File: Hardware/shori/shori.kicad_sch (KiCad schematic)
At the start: 127 parts, among them J1 430450200, J2 SWD_Header, J3 UART_Header, J4 530480310, J5 Conn_01x03, J6 530480210, SW1 SW_SPDT, U1 CS4272, U2 STM32H750VBTx, U3 NE5532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

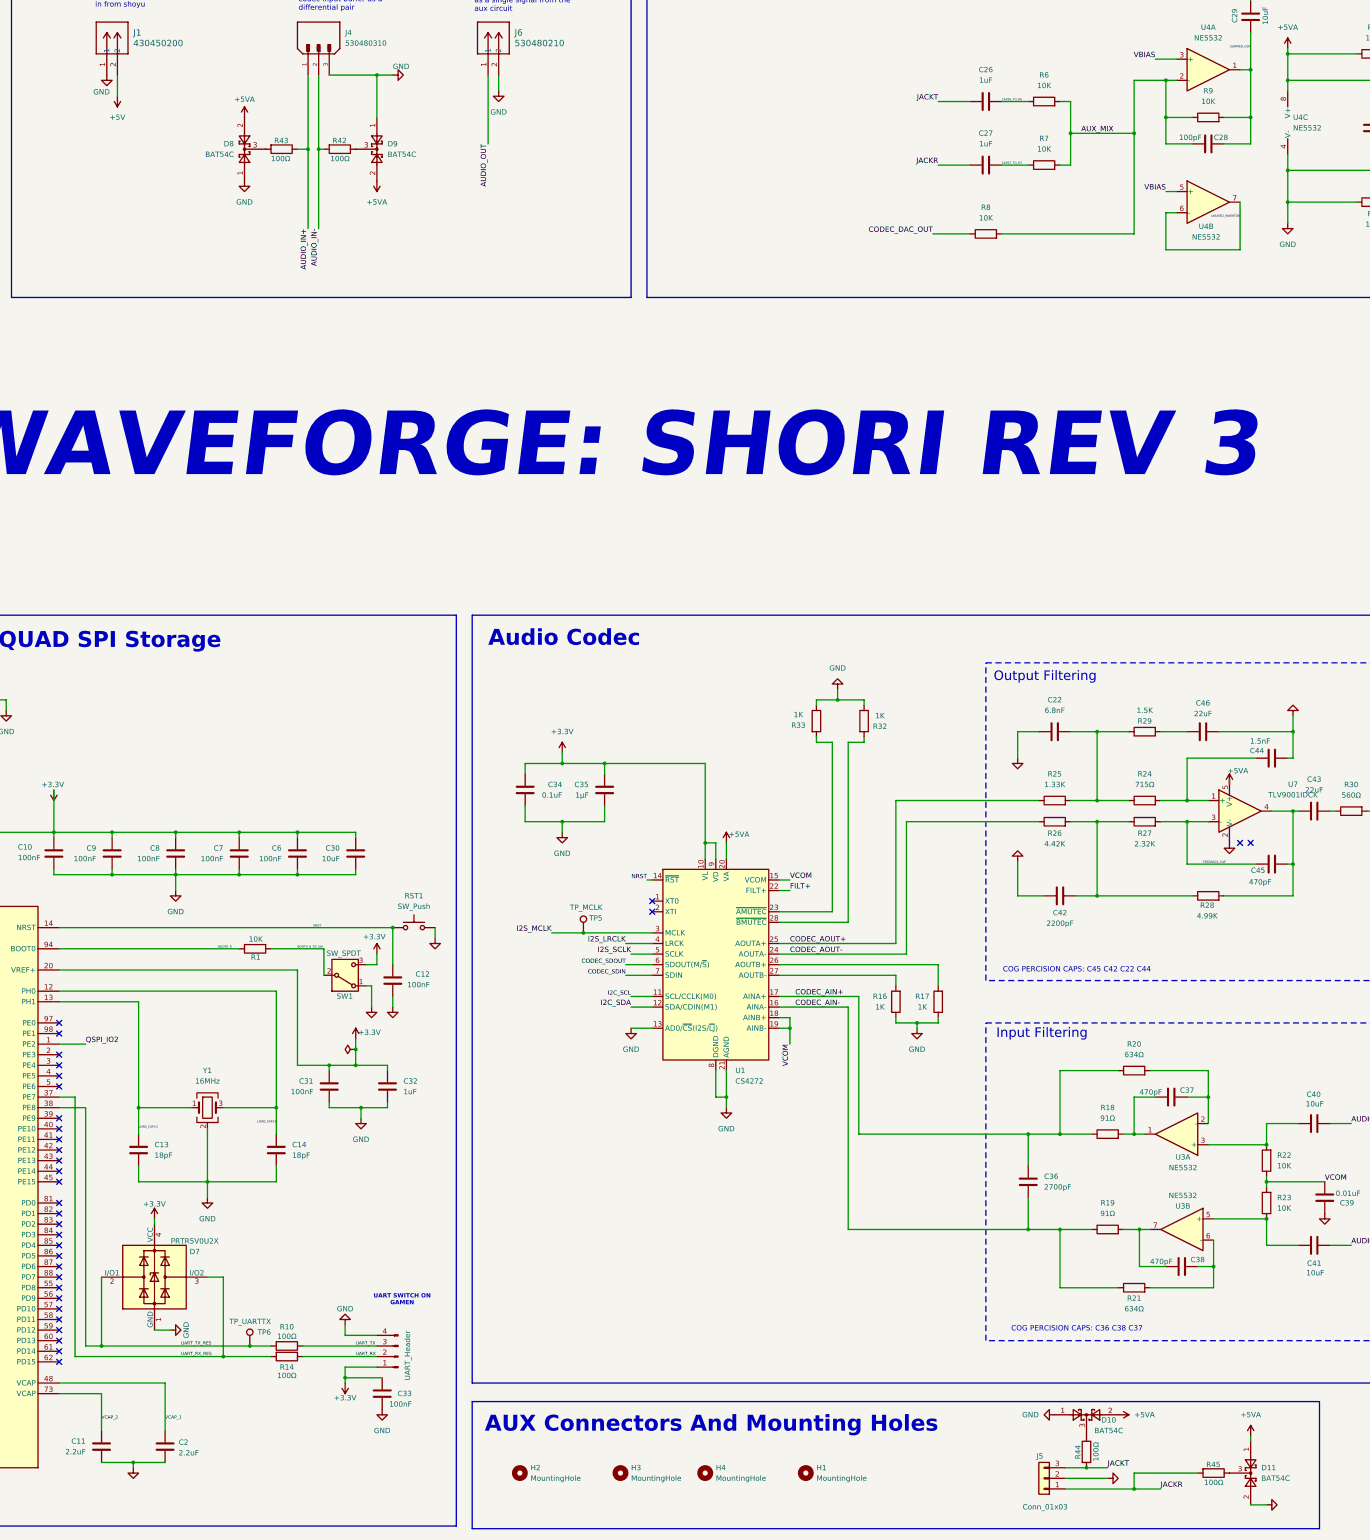
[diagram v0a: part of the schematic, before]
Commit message: Mae rev 1 schems done! power supply and audio out
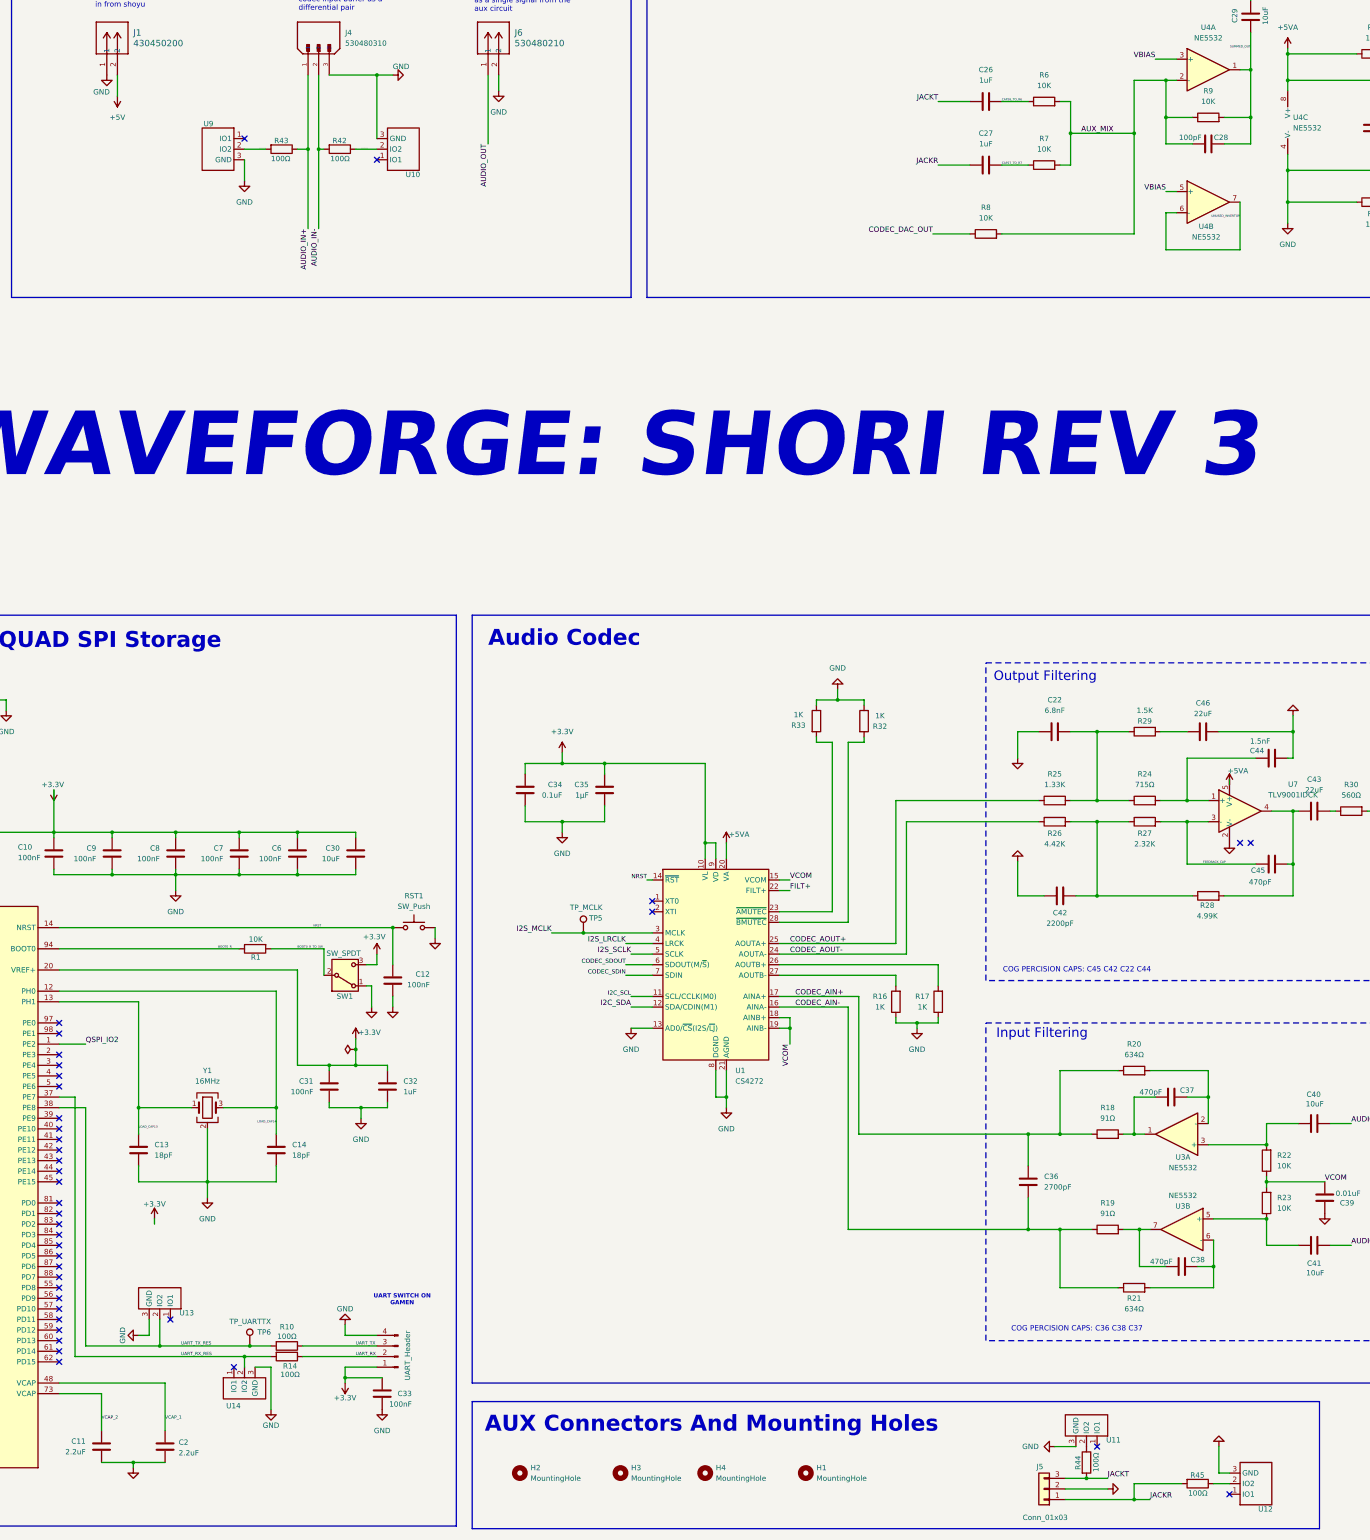
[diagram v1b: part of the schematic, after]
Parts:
- removed D10, D11, D8, D9: BAT54C, Package_TO_SOT_SMD:SOT-23, symbol Diode:BAT54C
- removed D7: PRTR5V0U2X, Package_TO_SOT_SMD:SOT-143, symbol Power_Protection:PRTR5V0U2X
- added U10, U11, U12, U13, U14, U9: (no value), Package_TO_SOT_SMD:SOT-23-3, symbol MyCrystal:ESDS452DBZRQ1
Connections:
- net GND: now also U10.3 (GND), U11.3 (GND), U12.3 (GND), U13.3 (GND), U14.3 (GND), U9.3 (GND)
- net SHUNT_RES_AINM: now also R42.1, U10.2 (IO2)
- net SHUNT_RES_AINP: now also U9.2 (IO2)
- net UART_RX_RES: now also U14.2 (IO2)
- net UART_TX_RES: now also U13.2 (IO2)
- net at R44.1: now also U11.2 (IO2)
- net at R45.1: now also U12.2 (IO2)
- no-connect marks 69 -> 75
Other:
- moved on the sheet: J5, R44, R45

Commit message: shori final touches!
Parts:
- added C50, C51: 10uF, Capacitor_SMD:C_0603_1608Metric_Pad1.08x0.95mm_HandSolder, symbol Device:C
- added J7: GROUND PROBE, Connector_PinSocket_2.00mm:PinSocket_1x02_P2.00mm_Vertical, symbol Connector:Conn_01x02_Socket
- Y1: footprint MyFootprints:XTAL_ABM8-12.288MHZ-B2-T -> Crystal:Crystal_SMD_3225-4Pin_3.2x2.5mm_HandSoldering
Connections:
- net +5VA: now also C50.2
- net GND: now also C50.1, C51.1, J7.1 (Pin_1), J7.2 (Pin_2)
- net VBIAS: now also C51.2
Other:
- moved on the sheet: C24, C25

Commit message: ongoing cart added
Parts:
- C1: footprint Capacitor_SMD:C_0603_1608Metric_Pad1.08x0.95mm_HandSolder -> Capacitor_SMD:C_0402_1005Metric_Pad0.74x0.62mm_HandSolder
- C20: value 0.1uF -> 100nF
- C4: footprint Capacitor_SMD:C_0402_1005Metric_Pad0.74x0.62mm_HandSolder -> Capacitor_SMD:C_0603_1608Metric_Pad1.08x0.95mm_HandSolder
- SW1: footprint Button_Switch_SMD:SW_SPDT_Shouhan_MSK12C02 -> Connector_PinHeader_2.54mm:PinHeader_1x03_P2.54mm_Vertical
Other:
- moved on the sheet: C10, C11, C12, C13, C14, C2, C30, C31, C32, C33, C47, C48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

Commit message: Shori: cleaned up flash and added more BOM
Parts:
- C17: value 10μF -> 10uF
- C19, C35: value 1μF -> 1uF
- C21, C34: value 0.1uF -> 100nF
- C47: footprint Capacitor_SMD:C_0402_1005Metric_Pad0.74x0.62mm_HandSolder -> Capacitor_SMD:C_0603_1608Metric_Pad1.08x0.95mm_HandSolder
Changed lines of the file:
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@@
 			)
 		)
-		(property "Value" "0.1uF"
+		(property "Value" "100nF"
 			(at 287.02 224.79 0)
 			(show_name no)
@@
 			)
 		)
-		(property "Value" "0.1uF"
-			(at 548.386 212.344 0)
+		(property "Value" "100nF"
+			(at 549.7061 212.3759 0)
 			(show_name no)
 			(do_not_autoplace no)
@@
 			)
 		)
-		(property "Value" "1μF"
+		(property "Value" "1uF"
 			(at 293.37 224.7899 0)
 			(show_name no)
@@
 			)
 		)
-		(property "Value" "10μF"
+		(property "Value" "10uF"
 			(at 546.1 294.6399 0)
 			(show_name no)
@@
 			)
 		)
-		(property "Value" "1μF"
+		(property "Value" "1uF"
 			(at 557.53 250.1899 0)
 			(show_name no)
@@
 			)
 		)
-		(property "Footprint" "Capacitor_SMD:C_0402_1005Metric_Pad0.74x0.62mm_HandSolder"
+		(property "Footprint" "Capacitor_SMD:C_0603_1608Metric_Pad1.08x0.95mm_HandSolder"
 			(at 48.5648 212.09 0)
 			(hide yes)

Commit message: Shori: Final BOM touches
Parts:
- C15: footprint MyFootprints:CAPPM3216X180N -> Capacitor_SMD:C_1206_3216Metric_Pad1.33x1.80mm_HandSolder
- Y1: value 16MHz -> 12.288MHz

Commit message: Remvoed 3.3V on shori UART and changed tantalum cap
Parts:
- removed C33: 100nF, Capacitor_SMD:C_0402_1005Metric_Pad0.74x0.62mm_HandSolder, symbol Device:C
- removed J2: SWD_Header, Connector_PinHeader_2.54mm:PinHeader_1x04_P2.54mm_Vertical, symbol Connector:Conn_01x04_Pin
- removed J6: 530480210, My footprints:CONN02_530480210_MOL, symbol 2 Pin Audio Molex:530480210
- removed U8: MAX40200AUK, Package_TO_SOT_SMD:SOT-23-5, symbol Analog_Switch:MAX40200AUK
- added C16: 10nF, Capacitor_SMD:C_0402_1005Metric_Pad0.74x0.62mm_HandSolder, symbol Device:C
- added C52: 100pF, Capacitor_SMD:C_0402_1005Metric_Pad0.74x0.62mm_HandSolder, symbol Device:C
- added C53: 10uF, Capacitor_SMD:C_0805_2012Metric, symbol Device:C
- added J2: Conn_01x05_Pin, Connector_Molex:Molex_PicoBlade_53048-0510_1x05_P1.25mm_Horizontal, symbol Connector:Conn_01x05_Pin
- added J6: 530480310, MyFootprints:MOLEX_530480310, symbol Audio Molex:530480310
- added R46: 10K, Resistor_SMD:R_0402_1005Metric_Pad0.72x0.64mm_HandSolder, symbol Device:R
- added U15: (no value), Package_TO_SOT_SMD:SOT-23-3, symbol MyCrystal:ESDS452DBZRQ1
- C15: value 100uF -> 47uF
- C17, C29, C3, C30, C4, C40, C41, C47, C50, C51: footprint Capacitor_SMD:C_0603_1608Metric_Pad1.08x0.95mm_HandSolder -> Capacitor_SMD:C_0805_2012Metric
- C23, C43, C46: footprint Capacitor_SMD:C_0805_2012Metric -> Capacitor_SMD:C_1206_3216Metric
- Y1: footprint Crystal:Crystal_SMD_3225-4Pin_3.2x2.5mm_HandSoldering -> Crystal:Crystal_SMD_3225-4Pin_3.2x2.5mm
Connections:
- net 5V_PROTECTED is gone; now on net +5V: C3.1, R40.2, TP1.1, U5.1 (IN), U5.5 (EN)
- net +3.3V: now also J2.5 (Pin_5); no longer J3.1 (Pin_1)
- net +5V: now also U15.1 (IO1), U15.2 (IO2)
- net GND: now also J3.1 (Pin_1), C16.1, J2.1 (Pin_1), J6.3, U15.3 (GND); no longer J3.4 (Pin_4)
- net NRST: now also J2.2 (Pin_2)
- net SHUNT_RES_AINM: now also U10.1 (IO1); no longer U10.2 (IO2)
- net SHUNT_RES_AINP: now also U9.1 (IO1); no longer U9.2 (IO2)
- net SWCLK: now also J2.3 (Pin_3)
- net SWDIO: now also J2.4 (Pin_4)
- net at U5.4 (NR/FB): now also C16.2
- net AUDIO_OUT renamed AUDIO_OUT+
- net AUDIO_OUT+: now also J6.1
- net SUMMED_OUT renamed SUMMED_OUT+
- net SUMMED_OUT+: now also U4.6 (-), C52.1, R46.1
- net UNUSED_INVERTOR renamed SUMMED_OUT-
- net SUMMED_OUT-: now also C52.2, C53.1, R46.2; no longer U4.6 (-)
- new net AUDIO_OUT-: C53.2, J6.2
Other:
- note added: "Audio Goes back to shoyu as a differntial signal from the aux circuit"
- note added: "WAVEFORGE: SHORI REV 4"
- note removed: "Audio Goes back to shoyu as a single signal from the aux circuit"
- note removed: "WAVEFORGE: SHORI REV 3"
- moved on the sheet: C24, C25, C26, C27, C28, C29, C50, C51, J1, J4, R4, R42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

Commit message: Created Gallery Folders
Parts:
- C15: footprint Capacitor_SMD:C_1206_3216Metric_Pad1.33x1.80mm_HandSolder -> MyFootprints:CAPMP6.3X3.2_2.8N_KEM
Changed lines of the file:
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@@
 			)
 		)
-		(property "Footprint" "Capacitor_SMD:C_1206_3216Metric_Pad1.33x1.80mm_HandSolder"
+		(property "Footprint" "MyFootprints:CAPMP6.3X3.2_2.8N_KEM"
 			(at 546.1 334.01 0)
 			(hide yes)
